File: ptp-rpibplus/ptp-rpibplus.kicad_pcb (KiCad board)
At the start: 2 copper layers, 65.5 x 56.6 mm, 9 parts, among them J1 RASPI_B+, J2 MODULE_HEADER, J3 MODULE_HEADER

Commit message: mostly happy. power and ground left.
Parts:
- moved C1 25.9 mm to (105.4, 102.9)
- moved C2 25.9 mm to (104.9, 104.6)
- moved C3 25.9 mm to (104.9, 105.9)
- moved J3 5.32 mm to (141.4, 115.0), turned to 315 degrees
- moved J2 2.99 mm to (119.7, 93.3), turned to 315 degrees
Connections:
- J2 pad 5: /CLK -> /SCK
- J3 pad 5: /CLK -> /SCK
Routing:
- net /B_G3: track 0.00 -> 59.9 mm, vias 0 -> 1
- net /B_G2/RX: track 0.00 -> 58.6 mm, vias 0 -> 1
- net /B_G1/TX: track 0.00 -> 57.3 mm, vias 0 -> 1
- net /SCL: track 0.00 -> 51.0 mm, vias 0 -> 1
- net /SDA: track 0.00 -> 49.3 mm
- net /SCK: track 0.00 -> 48.7 mm, vias 0 -> 1
- net /MOSI: track 0.00 -> 48.3 mm, vias 0 -> 2
- net /MISO: track 0.00 -> 48.0 mm, vias 0 -> 2
- net 3V3: track 39.3 -> 0.00 mm
- net /A_G3: track 0.00 -> 33.4 mm, vias 0 -> 1
- net /A_G1/TX: track 0.00 -> 29.9 mm
- net /A_G2/RX: track 0.00 -> 27.3 mm
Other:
- outline, holes or cut-outs redrawn
- rule trace_min: 0.254 -> 0.2032

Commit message: really really close
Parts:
- moved C3 19.5 mm to (102.1, 86.6), turned to 0 degrees
- moved C1 18.9 mm to (103.6, 84.1)
- moved C2 18.0 mm to (104.6, 86.6)
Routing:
- net GND: track 0.00 -> 514.4 mm, vias 0 -> 32
- net 3V3: track 0.00 -> 78.9 mm
- net /A_G1/TX: track 29.9 -> 24.7 mm
- net /SDA: track 49.3 -> 51.7 mm
- net /A_G2/RX: track 27.3 -> 26.2 mm
- net /SCL: track 51.0 -> 50.2 mm
- added copper zone on B.Cu, net GND
- added copper zone on F.Cu, net GND
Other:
- net class Default: via_dia 0.889 -> 1.016
- rule pad_to_mask_clearance: 0 -> 0.0762
- rule via_min_size: 0.889 -> 1.016

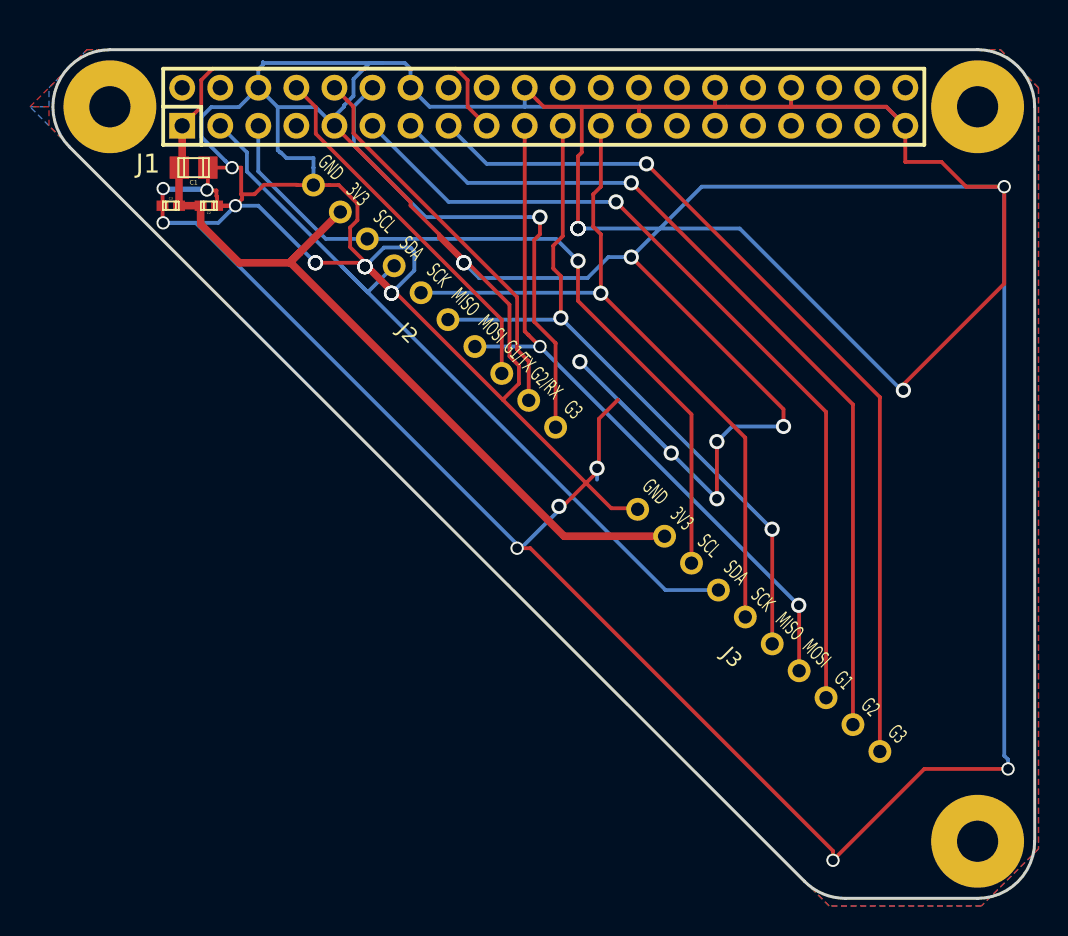
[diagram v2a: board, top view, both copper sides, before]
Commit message: stupid not-polygons are stupid
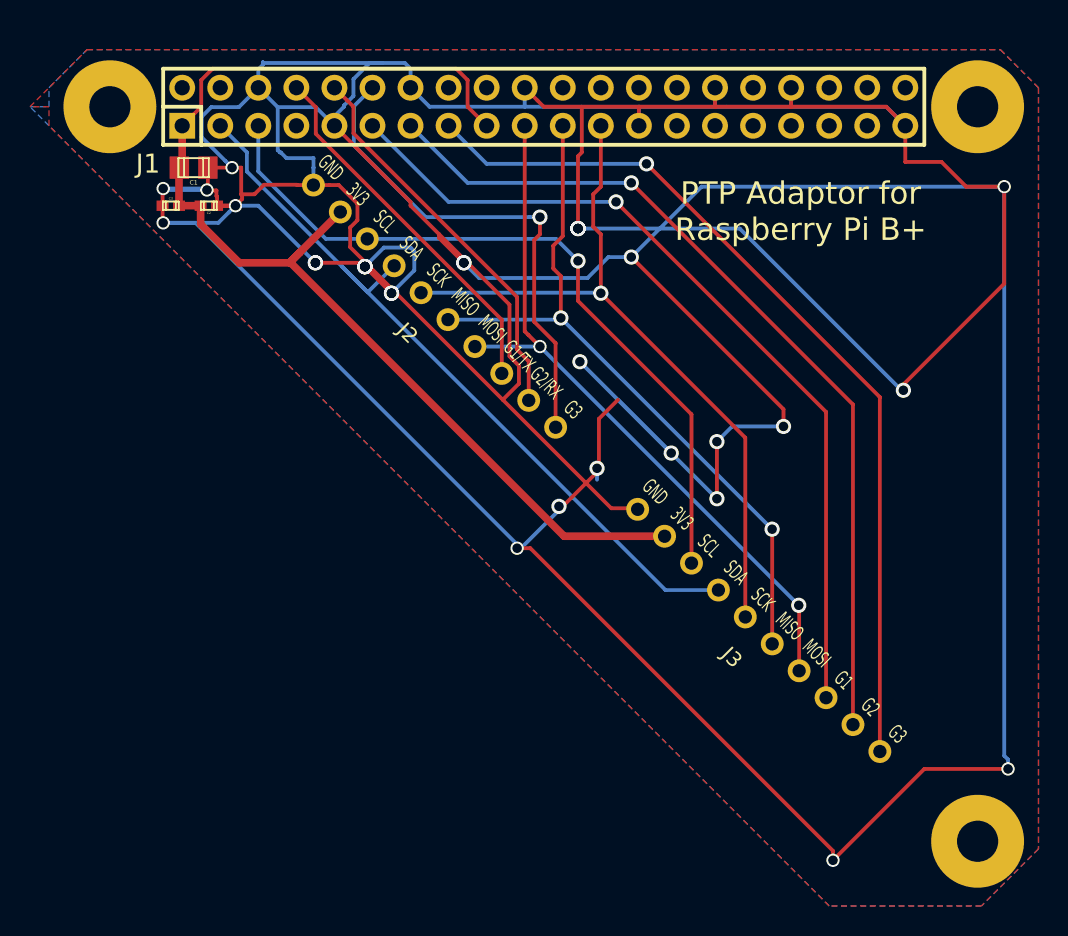
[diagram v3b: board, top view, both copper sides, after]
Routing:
- net GND: track 514.4 -> 491.5 mm
- net (no net): track 0.00 -> 23.0 mm
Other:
- board outline removed
- board text added: "PTP Adaptor for Raspberry Pi B+"

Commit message: mvp
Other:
- board outline added: 65.5 x 56.6 mm
